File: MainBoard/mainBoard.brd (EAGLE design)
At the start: 149.6 x 99.3 mm, 103 parts, among them IC2 74HC238, IC3 74HC151D, J1 22-05-7038-03, J2 22-05-7038-03, J3 22-05-7038-03, J4 22-05-7038-03, J5 22-05-7038-03, J6 22-05-7038-03, J7 22-05-7038-03, J8 22-05-7038-03, Q1 BC847ASMD, Q10 BC847ASMD, Q2 BC847ASMD, Q5 BC847ASMD, Q6 BC847ASMD, Q9 BC847ASMD, U1 STM32F0DISCOVERY, X1 PWR12, X2 MSTBA2, X3 MSTBA2, X4 MSTBA2, X5 MSTBA2, X6 MSTBA2, X7 MSTBA2

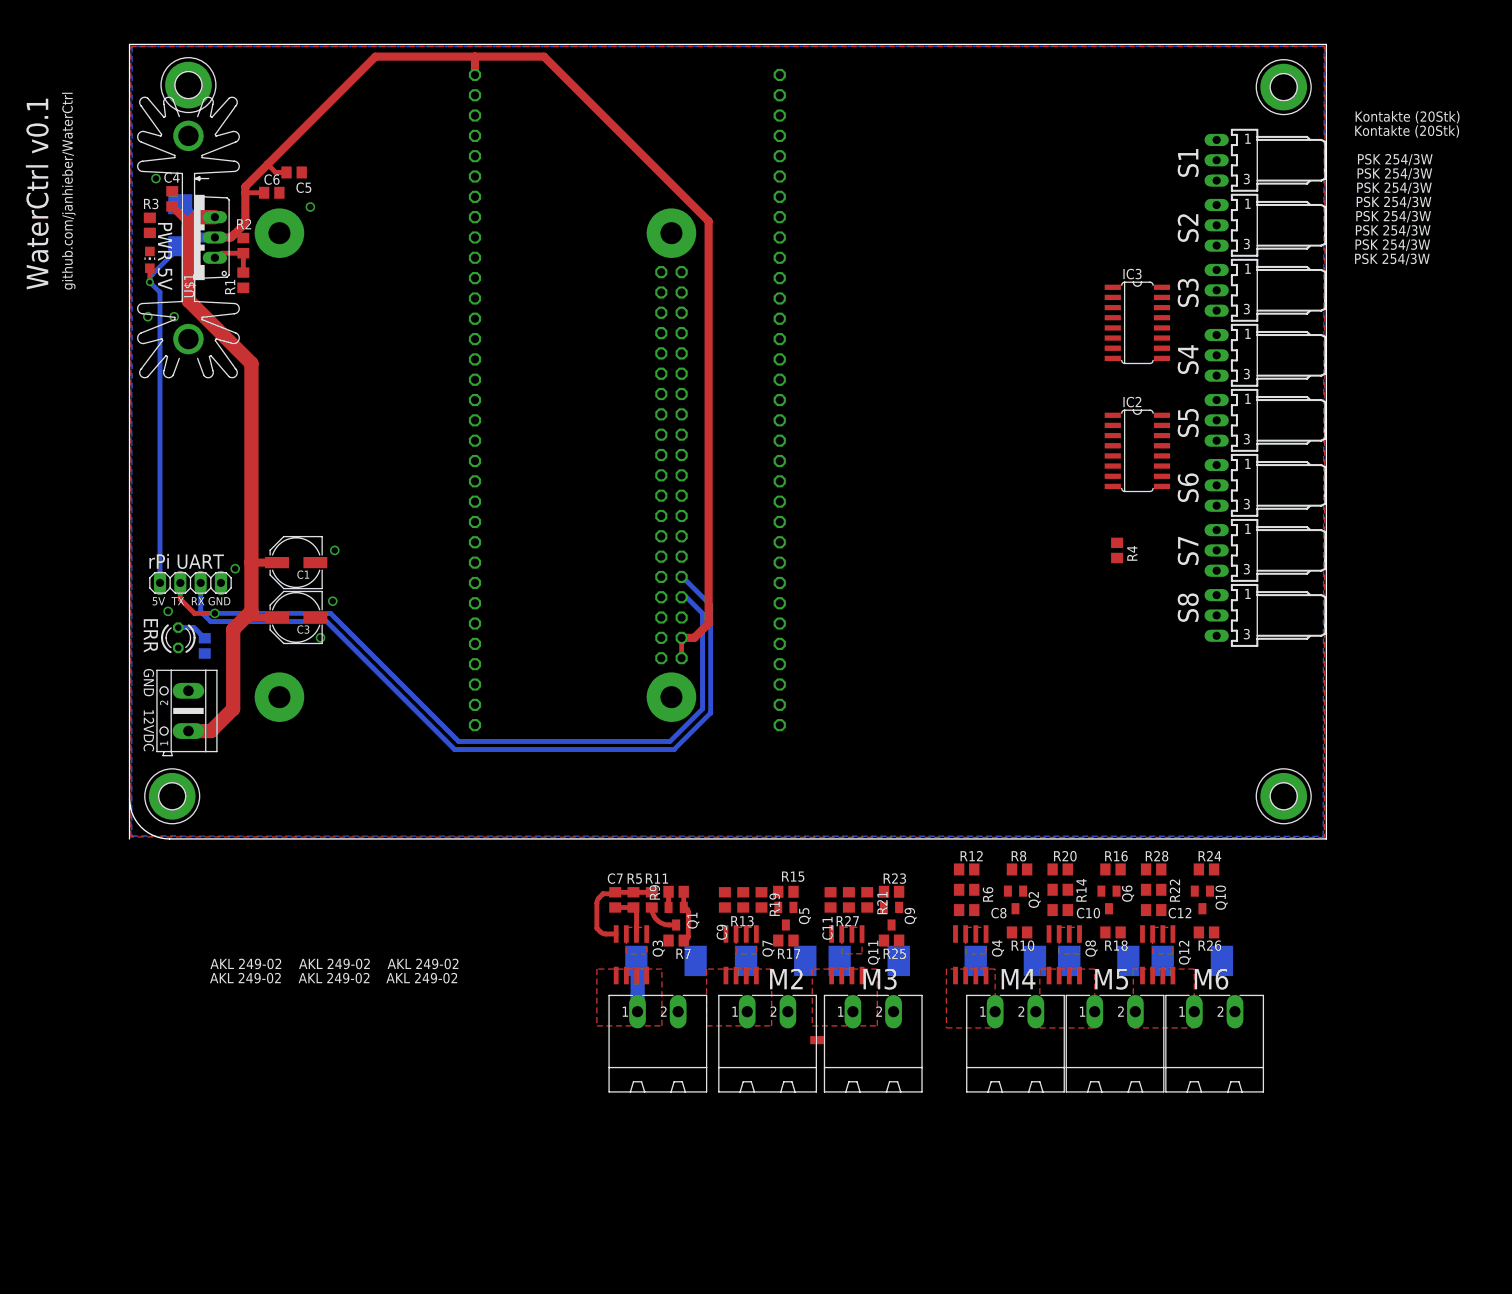
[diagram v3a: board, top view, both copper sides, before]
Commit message: board STM32 update
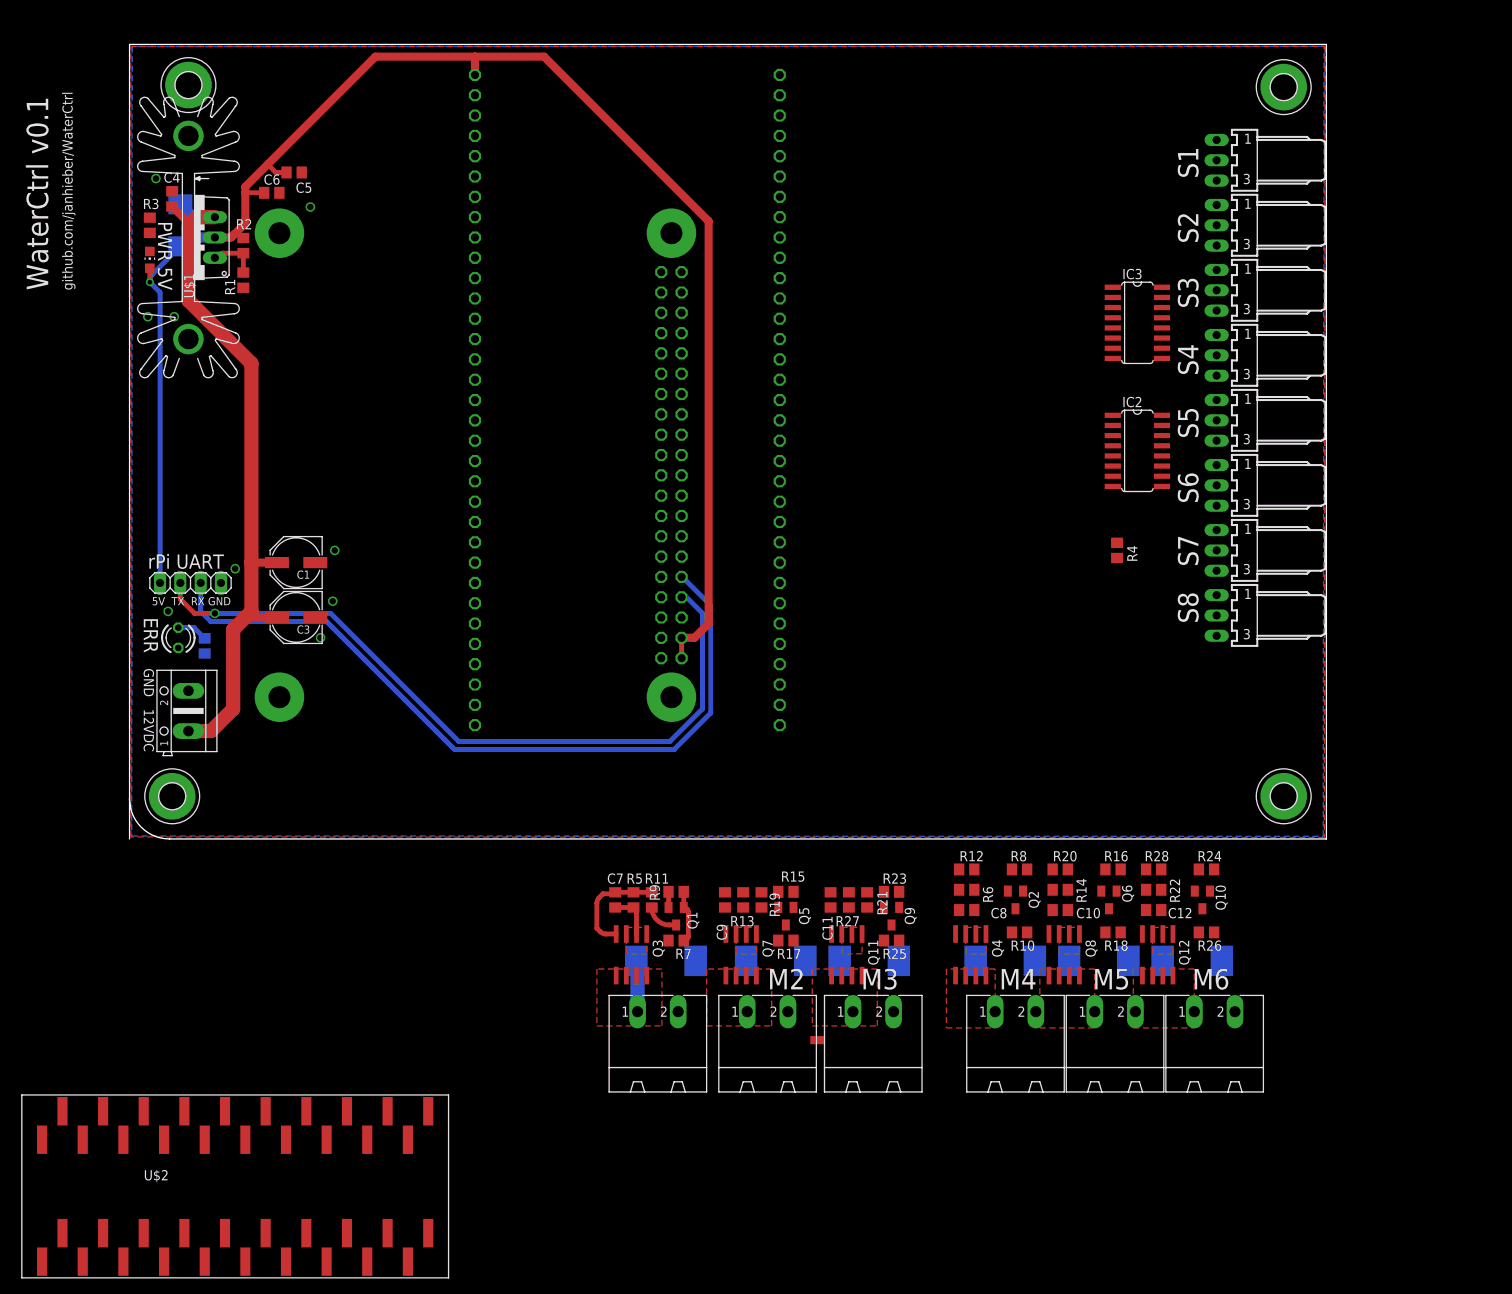
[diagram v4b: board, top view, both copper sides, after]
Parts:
- removed U$10, U$11: Kontakte (20Stk), extra:DUMMY_BOM
- removed U$12, U$13, U$14, U$15, U$16, U$17: AKL 249-02, extra:DUMMY_BOM
- removed U$3, U$4, U$5, U$6, U$7, U$8, U$9: PSK 254/3W, extra:DUMMY_BOM
- U$2: value PSK 254/3W -> STM32F103C8T6_DEV; device extra:DUMMY_BOM -> extra:STM32F103C8T6_DEV_SMD
- moved U$2 209.3 mm to (-13.5, -54.9)
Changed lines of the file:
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@@
 <?xml version="1.0" encoding="utf-8"?>
 <!DOCTYPE eagle SYSTEM "eagle.dtd">
-<eagle version="6.4">
+<eagle version="6.5.0">
 <drawing>
 <settings>
@@
 <attribute name="R" value="SMD-0805 100" x="9.398" y="24.13" size="1.778" layer="28" rot="MR90" display="off"/>
 </element>
-<element name="U$2" library="extra" package="DUMMY_BOM" value="PSK 254/3W" x="153.0356375" y="71.882"/>
-<element name="U$3" library="extra" package="DUMMY_BOM" value="PSK 254/3W" x="153.08753125" y="73.66"/>
-<element name="U$4" library="extra" package="DUMMY_BOM" value="PSK 254/3W" x="153.139425" y="75.438"/>
-<element name="U$5" library="extra" package="DUMMY_BOM" value="PSK 254/3W" x="153.19131875" y="77.216"/>
-<element name="U$6" library="extra" package="DUMMY_BOM" value="PSK 254/3W" x="153.2432125" y="78.994"/>
-<element name="U$7" library="extra" package="DUMMY_BOM" value="PSK 254/3W" x="153.29510625" y="80.772"/>
-<element name="U$8" library="extra" package="DUMMY_BOM" value="PSK 254/3W" x="153.347" y="82.55"/>
-<element name="U$9" library="extra" package="DUMMY_BOM" value="PSK 254/3W" x="153.39889375" y="84.328"/>
-<element name="U$12" library="extra" package="DUMMY_BOM" value="AKL 249-02" x="32.09068125" y="-18.034"/>
-<element name="U$13" library="extra" package="DUMMY_BOM" value="AKL 249-02" x="10.044575" y="-18.034"/>
-<element name="U$14" library="extra" package="DUMMY_BOM" value="AKL 249-02" x="10.09646875" y="-16.256"/>
-<element name="U$15" library="extra" package="DUMMY_BOM" value="AKL 249-02" x="32.2463625" y="-16.256"/>
-<element name="U$16" library="extra" package="DUMMY_BOM" value="AKL 249-02" x="21.12225625" y="-18.034"/>
-<element name="U$17" library="extra" package="DUMMY_BOM" value="AKL 249-02" x="21.17415" y="-16.256"/>
-<element name="U$10" library="extra" package="DUMMY_BOM" value="Kontakte (20Stk)" x="153.05204375" y="87.884"/>
-<element name="U$11" library="extra" package="DUMMY_BOM" value="Kontakte (20Stk)" x="153.1039375" y="89.662"/>
 <element name="PCB1" library="RASPBERRY_PI_Bplus" package="RASPBERRY_PI_BPLUS_TPLACE" value="RASPBERRY_PI_B+_TPLACE" x="15.24" y="14.224" rot="MR90"/>
 <element name="U$1" library="extra" package="TO220" value="LM350" x="8.128" y="75.184" smashed="yes" rot="R90">
@@
 <attribute name="VALUE" x="2.54" y="28.829" size="1.27" layer="27"/>
 </element>
+<element name="U$2" library="extra" package="STM32F103C8T6_DEV_SMD" value="STM32F103C8T6_DEV" x="-13.462" y="-54.864"/>
 </elements>
 <signals>
@@
 <via x="2.286" y="65.278" extent="1-16" drill="0.8"/>
 <via x="3.302" y="82.55" extent="1-16" drill="0.8"/>
+<wire x1="135.89" y1="74.168" x2="135.89" y2="82.296" width="0" layer="19" extent="1-1"/>
+<wire x1="135.89" y1="66.04" x2="135.89" y2="74.168" width="0" layer="19" extent="1-1"/>
+<wire x1="135.89" y1="57.912" x2="135.89" y2="66.04" width="0" layer="19" extent="1-1"/>
+<wire x1="135.89" y1="49.784" x2="135.89" y2="57.912" width="0" layer="19" extent="1-1"/>
+<wire x1="135.89" y1="41.656" x2="135.89" y2="49.784" width="0" layer="19" extent="1-1"/>
+<wire x1="135.89" y1="33.528" x2="135.89" y2="41.656" width="0" layer="19" extent="1-1"/>
+<wire x1="135.89" y1="25.4" x2="135.89" y2="33.528" width="0" layer="19" extent="1-1"/>
+<wire x1="122.9106" y1="60.071" x2="135.89" y2="57.912" width="0" layer="19" extent="1-1"/>
+<wire x1="122.9106" y1="44.069" x2="135.89" y2="41.656" width="0" layer="19" extent="1-1"/>
+<wire x1="133.162" y1="-6.52" x2="135.89" y2="25.4" width="0" layer="19" extent="1-1"/>
 <wire x1="133.67" y1="-11.684" x2="133.162" y2="-6.52" width="0" layer="19" extent="1-1"/>
 <wire x1="136.542" y1="-15.24" x2="133.67" y2="-11.684" width="0" layer="19" extent="1-16"/>
@@
 <wire x1="67.376" y1="-8.552" x2="70.756" y2="-15.24" width="0" layer="19" extent="1-16"/>
 <wire x1="81.28" y1="14.224" x2="81.092" y2="-8.552" width="0" layer="19" extent="1-1"/>
+<wire x1="69.01" y1="27.674" x2="81.28" y2="14.224" width="0" layer="19" extent="1-1"/>
+<wire x1="66.47" y1="32.754" x2="69.01" y2="27.674" width="0" layer="19" extent="1-1"/>
+<wire x1="69.01" y1="37.834" x2="66.47" y2="32.754" width="0" layer="19" extent="1-1"/>
+<wire x1="69.01" y1="45.454" x2="69.01" y2="37.834" width="0" layer="19" extent="1-1"/>
+<wire x1="66.47" y1="53.074" x2="69.01" y2="45.454" width="0" layer="19" extent="1-1"/>
+<wire x1="69.01" y1="58.154" x2="66.47" y2="53.074" width="0" layer="19" extent="1-1"/>
+<wire x1="69.01" y1="63.234" x2="69.01" y2="58.154" width="0" layer="19" extent="1-1"/>
+<wire x1="66.47" y1="70.854" x2="69.01" y2="63.234" width="0" layer="19" extent="1-1"/>
+<wire x1="81.28" y1="75.184" x2="66.47" y2="70.854" width="0" layer="19" extent="1-1"/>
+<wire x1="81.28" y1="92.964" x2="81.28" y2="75.184" width="0" layer="19" extent="1-1"/>
+<wire x1="43.18" y1="14.224" x2="69.01" y2="27.674" width="0" layer="19" extent="1-1"/>
+<wire x1="23.876" y1="25.146" x2="43.18" y2="14.224" width="0" layer="19" extent="1-1"/>
+<wire x1="23.228" y1="27.686" x2="23.876" y2="25.146" width="0" layer="19" extent="1-1"/>
+<wire x1="25.4" y1="29.718" x2="23.228" y2="27.686" width="0" layer="19" extent="1-1"/>
+<wire x1="23.228" y1="34.544" x2="25.4" y2="29.718" width="0" layer="19" extent="1-1"/>
+<wire x1="25.654" y1="36.068" x2="23.228" y2="34.544" width="0" layer="19" extent="1-1"/>
+<wire x1="13.208" y1="33.782" x2="23.228" y2="34.544" width="0" layer="19" extent="1-1"/>
+<wire x1="11.43" y1="32.004" x2="13.208" y2="33.782" width="0" layer="19" extent="1-1"/>
+<wire x1="4.826" y1="28.448" x2="11.43" y2="32.004" width="0" layer="19" extent="1-1"/>
+<wire x1="9.398" y1="23.18" x2="4.826" y2="28.448" width="0" layer="19" extent="16-16"/>
+<wire x1="7.366" y1="18.5166" x2="9.398" y2="23.18" width="0" layer="19" extent="16-16"/>
+<wire x1="43.18" y1="92.964" x2="66.47" y2="70.854" width="0" layer="19" extent="1-1"/>
+<wire x1="21.524" y1="83.312" x2="43.18" y2="92.964" width="0" layer="19" extent="1-1"/>
+<wire x1="18.73" y1="80.772" x2="21.524" y2="83.312" width="0" layer="19" extent="1-1"/>
+<wire x1="22.606" y1="78.994" x2="18.73" y2="80.772" width="0" layer="19" extent="1-1"/>
+<wire x1="14.224" y1="68.9" x2="18.73" y2="80.772" width="0" layer="19" extent="1-1"/>
+<wire x1="5.588" y1="65.278" x2="14.224" y2="68.9" width="0" layer="19" extent="1-1"/>
+<wire x1="2.286" y1="65.278" x2="5.588" y2="65.278" width="0" layer="19" extent="1-1"/>
+<wire x1="2.54" y1="77.658" x2="2.286" y2="65.278" width="0" layer="19" extent="1-1"/>
+<wire x1="5.334" y1="80.96" x2="2.54" y2="77.658" width="0" layer="19" extent="1-1"/>
+<wire x1="3.302" y1="82.55" x2="5.334" y2="80.96" width="0" layer="19" extent="1-1"/>
 </signal>
 <signal name="N$29">

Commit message: board updates, rpi and stm32
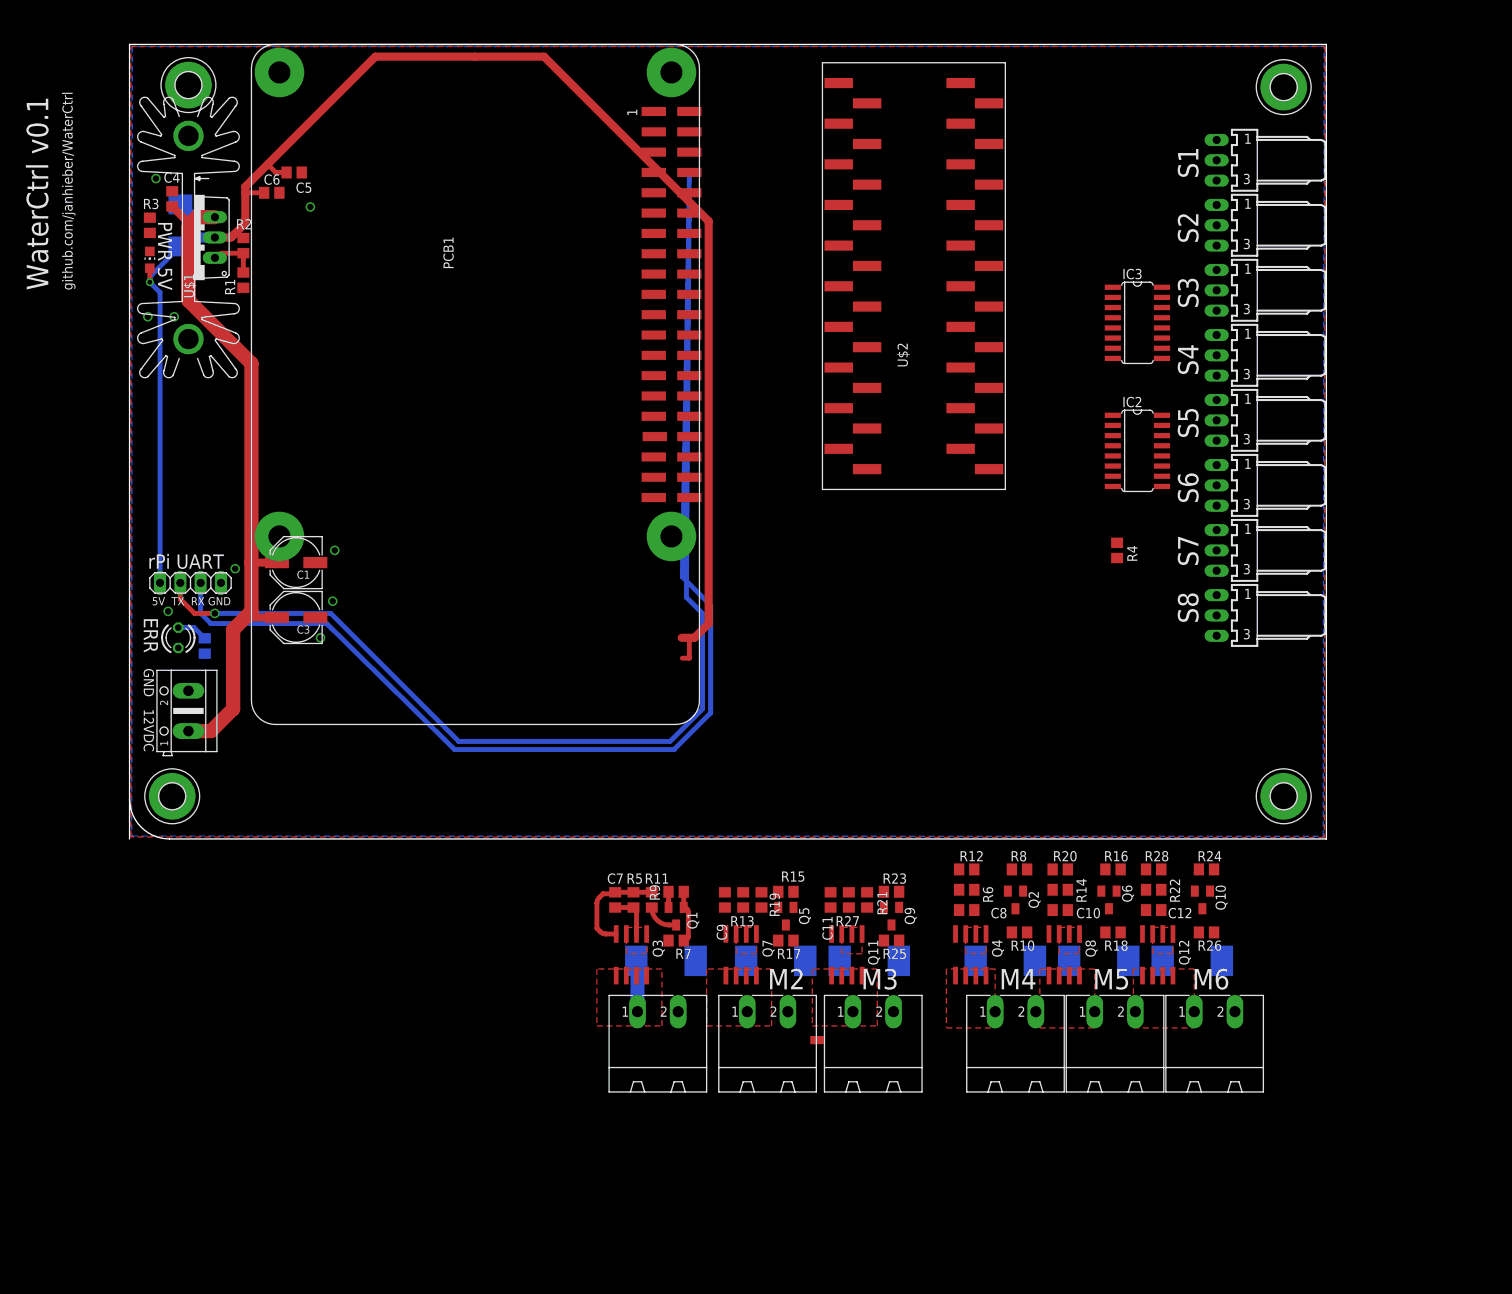
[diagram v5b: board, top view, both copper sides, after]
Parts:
- removed U1: STM32F0DISCOVERY, extra:STM32F0DISCOVERY
- PCB1: value RASPBERRY_PI_B+_TPLACE -> RASPBERRY_PI_B+; device RASPBERRY_PI_Bplus:RASPBERRY_PI_BPLUS_TPLACE -> RASPBERRY_PI_Bplus:RASPBERRY_PI_BPLUS_TPLACE_SMD_MIRR
- moved U$2 157.6 mm to (109.5, 43.7), turned to 90 degrees
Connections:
- new net 5V: U$2.P$3
- net +3V3: no longer U1.1
- net +5V: now also PCB1.P$2, PCB1.P$4; no longer PCB1.2, PCB1.4, U1.66
- net 3V3: now also PCB1.P$1, PCB1.P$17, U$2.P$1, U$2.P$23; no longer PCB1.1, PCB1.17
- net GND: now also PCB1.P$14, PCB1.P$20, PCB1.P$25, PCB1.P$30, PCB1.P$34, PCB1.P$39, PCB1.P$6, PCB1.P$9, U$2.P$2, U$2.P$21, U$2.P$22; no longer PCB1.14, PCB1.20, PCB1.25, PCB1.30, PCB1.34, PCB1.39, PCB1.6, PCB1.9, U1.2, U1.33, U1.34, U1.65, U1.9
- net RPI_RXD: now also PCB1.P$10; no longer PCB1.10
- net RPI_TXD: now also PCB1.P$8; no longer PCB1.8
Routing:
- net RPI_TXD: track 91.8 -> 144.3 mm
- net RPI_RXD: track 94.9 -> 142.9 mm
- net +5V: track 198.5 -> 198.0 mm

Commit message: board updates
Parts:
- moved PCB1 85.1 mm to (17.5, 99.3), flipped to the top, turned to 270 degrees
- moved U$2 79.9 mm to (35.3, 73.4), turned to 270 degrees
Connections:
- new net N$23: PCB1.1
- net +5V: now also PCB1.2, PCB1.4; no longer PCB1.P$2, PCB1.P$4
- net 3V3: now also PCB1.17, U$2.1, U$2.23; no longer PCB1.P$1, PCB1.P$17, U$2.P$1, U$2.P$23
- net 5V: now also U$2.3; no longer U$2.P$3
- net GND: now also PCB1.14, PCB1.20, PCB1.25, PCB1.30, PCB1.34, PCB1.39, PCB1.6, PCB1.9, U$2.2, U$2.21, U$2.22; no longer PCB1.P$14, PCB1.P$20, PCB1.P$25, PCB1.P$30, PCB1.P$34, PCB1.P$39, PCB1.P$6, PCB1.P$9, U$2.P$2, U$2.P$21, U$2.P$22
- net RPI_RXD: now also PCB1.10; no longer PCB1.P$10
- net RPI_TXD: now also PCB1.8; no longer PCB1.P$8
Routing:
- net RPI_TXD: track 144.3 -> 0.00 mm, vias 1 -> 0
- net +5V: track 198.0 -> 70.0 mm
- net RPI_RXD: track 142.9 -> 20.1 mm
